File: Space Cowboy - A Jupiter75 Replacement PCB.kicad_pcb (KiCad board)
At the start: 2 copper layers, 303.5 x 119.5 mm, 237 parts, among them SW1 SW_PUSH, U1 ATmega32U4-AU, Y1 16MHz

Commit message: Update Space Cowboy - A Jupiter75 Replacement PCB.kicad_pcb
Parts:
- moved R4 46.2 mm to (160.3, 147.3), turned to 0 degrees
- moved C8 0.33 mm to (164.8, 144.3)
- moved C6 0.28 mm to (166.1, 153.8), turned to 0 degrees
- moved C7 0.28 mm to (166.1, 147.4)
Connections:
- DRGB1 pad 4DIN: RGB_DI_PIN -> (no net)
- DRGB18 pad 4DIN: (no net) -> RGB_DI_PIN
- U1 pad 10: ROW1 -> ROW0
- U1 pad 11: ROW2 -> ROW1
- U1 pad 9: ROW0 -> ROW2
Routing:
- net ROW0: track 285.8 -> 378.7 mm, vias 0 -> 2
- net ROW1: track 290.1 -> 360.3 mm, vias 0 -> 2
- net Net-(R4-Pad1): track 4.32 -> 62.0 mm, vias 0 -> 4
- net ROW2: track 276.8 -> 325.3 mm, vias 0 -> 2
- net ROW3: track 296.0 -> 330.0 mm, vias 0 -> 2
- net Net-(R2-Pad2): track 174.4 -> 200.6 mm, vias 2 -> 4
- net Net-(R3-Pad1): track 175.0 -> 200.9 mm, vias 2 -> 4
- net RGB_DI_PIN: track 0.00 -> 25.2 mm, vias 0 -> 2
- net ROW5: track 312.4 -> 336.1 mm, vias 2 -> 4
- net Net-(D46-Pad2): track 3.70 -> 20.5 mm, vias 0 -> 1
- net +5V: track 1139.8 -> 1154.1 mm, vias 12 -> 13
- net COL6: track 169.9 -> 157.1 mm
- net ROW4: track 296.5 -> 305.8 mm
- net GND: track 137.1 -> 142.1 mm
- net Net-(D31-Pad2): track 12.8 -> 14.0 mm, vias 0 -> 1
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- added copper zone on B.Cu, net GND

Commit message: Update Space Cowboy - A Jupiter75 Replacement PCB.kicad_pcb
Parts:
- moved R6 1.63 mm to (69.9, 52.6)
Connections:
- U1 pad TAB: (no net) -> GND
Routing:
- net GND: track 142.1 -> 516.7 mm, vias 2 -> 20
- net +5V: track 1154.1 -> 1165.3 mm
- net COL11: track 257.8 -> 255.8 mm
- net Net-(R6-Pad1): track 3.67 -> 5.29 mm
- net (no net): track 587.6 -> 586.8 mm
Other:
- board text added: "J.C.K. Revision 1.0 2021"

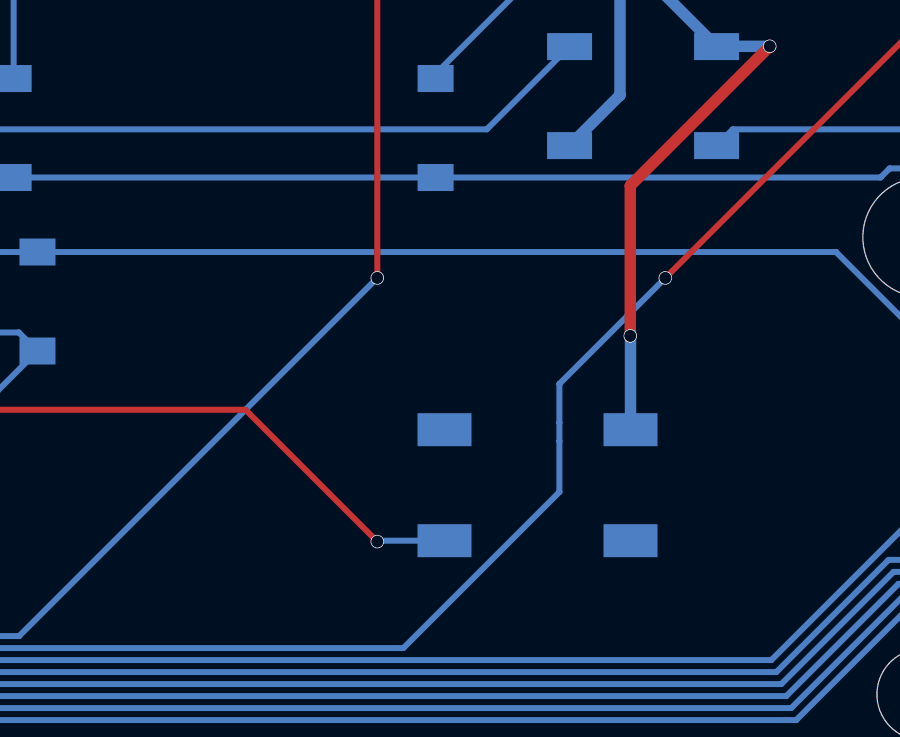
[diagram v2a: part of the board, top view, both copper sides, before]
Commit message: Update Space Cowboy - A Jupiter75 Replacement PCB.kicad_pcb
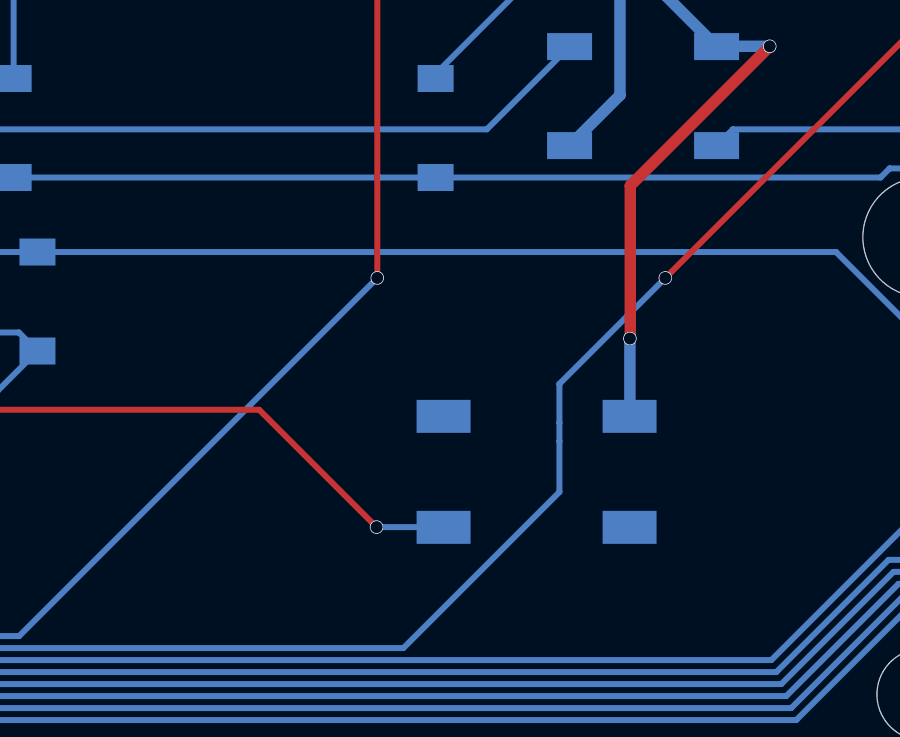
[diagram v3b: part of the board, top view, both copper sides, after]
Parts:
- added G***: LOGO, Graphics:Space Cowboy 2, B.Cu at (197.8, 159.4)
- moved SW1 0.45 mm to (213.5, 152.0)

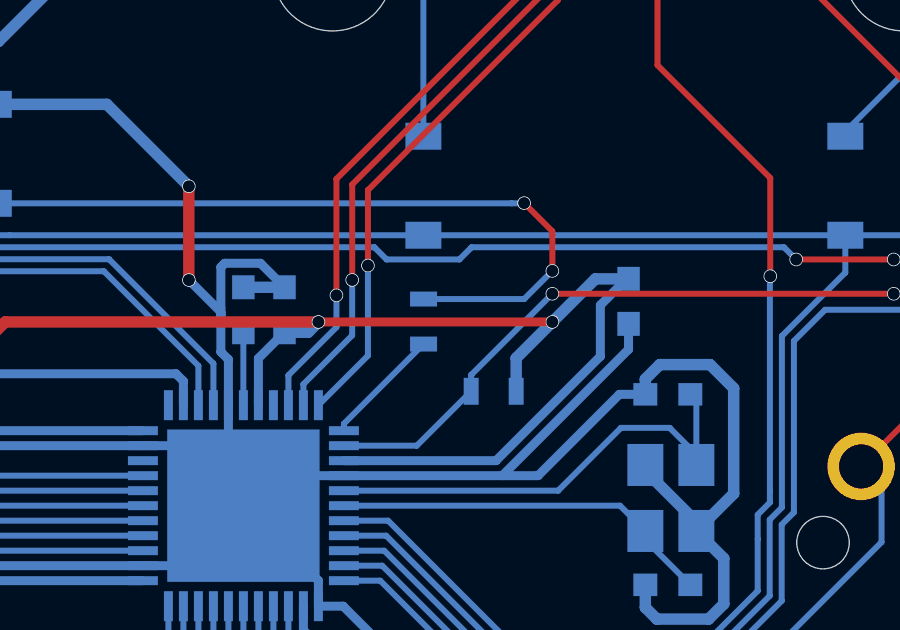
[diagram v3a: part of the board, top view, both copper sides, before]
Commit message: Update Space Cowboy - A Jupiter75 Replacement PCB.kicad_pcb
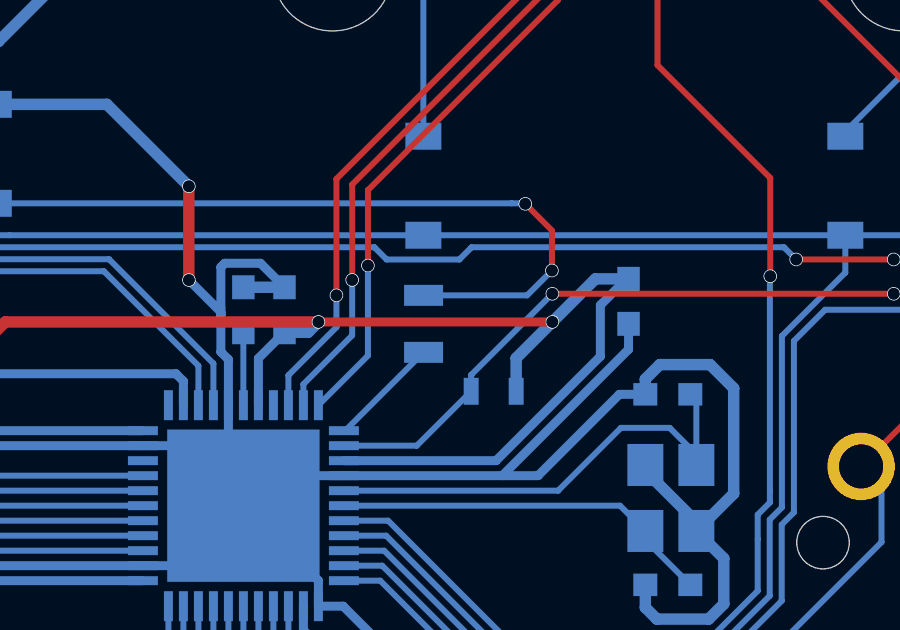
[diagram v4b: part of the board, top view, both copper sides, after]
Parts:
- R7: footprint Resistors_SMD:R_0603 -> Resistors_SMD:R_0805
- moved R7 0.08 mm to (158.0, 145.1)
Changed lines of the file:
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@@
     (thickness 1.6)
     (drawings 17)
-    (tracks 1684)
+    (tracks 1683)
     (zones 0)
     (modules 238)
@@
     (uvia_drill 0.1)
   )
+  (module Resistors_SMD:R_0805 (layer B.Cu)
+    (at 157.9626 145.0975 270)
+    (descr "Resistor SMD 0805, reflow soldering, Vishay (see dcrcw.pdf)")
+    (tags "resistor 0805")
+    (attr smd)
+    (fp_text reference R7 (at 0 1.45 90) (layer B.SilkS) hide
+      (effects (font (size 1 1) (thickness 0.15)) (justify mirror))
+    )
+    (fp_text value 0.5k (at 0 -1.5 90) (layer B.Fab) hide
+      (effects (font (size 1 1) (thickness 0.15)) (justify mirror))
+    )
+    (fp_line (start 1.55 -0.9) (end -1.55 -0.9) (layer B.CrtYd) (width 0.05))
+    (fp_line (start 1.55 -0.9) (end 1.55 0.9) (layer B.CrtYd) (width 0.05))
+    (fp_line (start -1.55 0.9) (end -1.55 -0.9) (layer B.CrtYd) (width 0.05))
+    (fp_line (start -1.55 0.9) (end 1.55 0.9) (layer B.CrtYd) (width 0.05))
+    (fp_line (start -0.6 0.88) (end 0.6 0.88) (layer B.SilkS) (width 0.12))
+    (fp_line (start 0.6 -0.88) (end -0.6 -0.88) (layer B.SilkS) (width 0.12))
+    (fp_line (start -1 0.62) (end 1 0.62) (layer B.Fab) (width 0.1))
+    (fp_line (start 1 0.62) (end 1 -0.62) (layer B.Fab) (width 0.1))
+    (fp_line (start 1 -0.62) (end -1 -0.62) (layer B.Fab) (width 0.1))
+    (fp_line (start -1 -0.62) (end -1 0.62) (layer B.Fab) (width 0.1))
+    (fp_text user %R (at 0.0007 0 90) (layer B.Fab)
+      (effects (font (size 0.4 0.4) (thickness 0.075)) (justify mirror))
+    )
+    (pad 1 smd rect (at -0.95 0 270) (size 0.7 1.3) (layers B.Cu B.Paste B.Mask)
+      (net 123 RGB_DI_PIN))
+    (pad 2 smd rect (at 0.95 0 270) (size 0.7 1.3) (layers B.Cu B.Paste B.Mask)
+      (net 124 "Net-(R7-Pad2)"))
+    (model ${KISYS3DMOD}/Resistors_SMD.3dshapes/R_0805.wrl
+      (at (xyz 0 0 0))
+      (scale (xyz 1 1 1))
+      (rotate (xyz 0 0 0))
+    )
+  )
   (module "Graphics:Space Cowboy 2" (layer B.Cu)
     (at 197.805 159.4485 180)
@@
   )
   (module Resistors_SMD:R_0603 (layer B.Cu)
-    (at 157.9626 145.0206 270)
-    (descr "Resistor SMD 0603, reflow soldering, Vishay (see dcrcw.pdf)")
-    (tags "resistor 0603")
-    (attr smd)
-    (fp_text reference R7 (at 0 1.45 90) (layer B.SilkS) hide
-      (effects (font (size 1 1) (thickness 0.15)) (justify mirror))
-    )
-    (fp_text value 0.5k (at 0 -1.5 90) (layer B.Fab)
-      (effects (font (size 1 1) (thickness 0.15)) (justify mirror))
-    )
-    (fp_line (start 1.25 -0.7) (end -1.25 -0.7) (layer B.CrtYd) (width 0.05))
-    (fp_line (start 1.25 -0.7) (end 1.25 0.7) (layer B.CrtYd) (width 0.05))
-    (fp_line (start -1.25 0.7) (end -1.25 -0.7) (layer B.CrtYd) (width 0.05))
-    (fp_line (start -1.25 0.7) (end 1.25 0.7) (layer B.CrtYd) (width 0.05))
-    (fp_line (start -0.5 0.68) (end 0.5 0.68) (layer B.SilkS) (width 0.12))
-    (fp_line (start 0.5 -0.68) (end -0.5 -0.68) (layer B.SilkS) (width 0.12))
-    (fp_line (start -0.8 0.4) (end 0.8 0.4) (layer B.Fab) (width 0.1))
-    (fp_line (start 0.8 0.4) (end 0.8 -0.4) (layer B.Fab) (width 0.1))
-    (fp_line (start 0.8 -0.4) (end -0.8 -0.4) (layer B.Fab) (width 0.1))
-    (fp_line (start -0.8 -0.4) (end -0.8 0.4) (layer B.Fab) (width 0.1))
-    (fp_text user %R (at 0.0007 0 90) (layer B.Fab)
-      (effects (font (size 0.4 0.4) (thickness 0.075)) (justify mirror))
-    )
-    (pad 1 smd rect (at -0.75 0 270) (size 0.5 0.9) (layers B.Cu B.Paste B.Mask)
-      (net 123 RGB_DI_PIN))
-    (pad 2 smd rect (at 0.75 0 270) (size 0.5 0.9) (layers B.Cu B.Paste B.Mask)
-      (net 124 "Net-(R7-Pad2)"))
-    (model ${KISYS3DMOD}/Resistors_SMD.3dshapes/R_0603.wrl
-      (at (xyz 0 0 0))
-      (scale (xyz 1 1 1))
-      (rotate (xyz 0 0 0))
-    )
-  )
-  (module Resistors_SMD:R_0603 (layer B.Cu)
     (at 69.862 52.6288)
     (descr "Resistor SMD 0603, reflow soldering, Vishay (see dcrcw.pdf)")
@@
   (segment (start 68.298 50.1892) (end 69.112 51.0032) (width 0.2) (layer B.Cu) (net 122))
   (segment (start 68.298 47.6746) (end 68.298 50.1892) (width 0.2) (layer B.Cu) (net 122))
-  (via (at 162.2552 143.3322) (size 0.45) (drill 0.4) (layers F.Cu B.Cu) (net 123))
-  (segment (start 161.3168 144.2706) (end 162.2552 143.3322) (width 0.2) (layer B.Cu) (net 123))
-  (segment (start 157.9626 144.2706) (end 161.3168 144.2706) (width 0.2) (layer B.Cu) (net 123))
-  (segment (start 162.2552 143.3322) (end 162.2552 142.1384) (width 0.2) (layer F.Cu) (net 123))
   (segment (start 143.4875 141.08) (end 160.9006 141.08) (width 0.2) (layer B.Cu) (net 123))
-  (via (at 161.3154 141.0716) (size 0.45) (drill 0.4) (layers F.Cu B.Cu) (net 123))
-  (segment (start 161.307 141.08) (end 161.3154 141.0716) (width 0.2) (layer B.Cu) (net 123))
-  (segment (start 160.9006 141.08) (end 161.307 141.08) (width 0.2) (layer B.Cu) (net 123))
-  (segment (start 162.2552 142.0114) (end 162.2552 142.1384) (width 0.2) (layer F.Cu) (net 123))
-  (segment (start 161.3154 141.0716) (end 162.2552 142.0114) (width 0.2) (layer F.Cu) (net 123))
-  (segment (start 155.3074 148.4258) (end 157.9626 145.7706) (width 0.2) (layer B.Cu) (net 124))
-  (segment (start 155.3074 148.6582) (end 155.3074 148.4258) (width 0.2) (layer B.Cu) (net 124))
+  (via (at 162.2425 143.3195) (size 0.45) (drill 0.4) (layers F.Cu B.Cu) (net 123))
+  (segment (start 161.4145 144.1475) (end 162.2425 143.3195) (width 0.2) (layer B.Cu) (net 123))
+  (segment (start 157.9626 144.1475) (end 161.4145 144.1475) (width 0.2) (layer B.Cu) (net 123))
+  (via (at 161.3535 141.097) (size 0.45) (drill 0.4) (layers F.Cu B.Cu) (net 123))
+  (segment (start 161.3365 141.08) (end 161.3535 141.097) (width 0.2) (layer B.Cu) (net 123))
+  (segment (start 160.9006 141.08) (end 161.3365 141.08) (width 0.2) (layer B.Cu) (net 123))
+  (segment (start 162.2425 141.986) (end 161.3535 141.097) (width 0.2) (layer F.Cu) (net 123))
+  (segment (start 162.2425 143.3195) (end 162.2425 141.986) (width 0.2) (layer F.Cu) (net 123))
+  (segment (start 155.3519 148.6582) (end 157.9626 146.0475) (width 0.2) (layer B.Cu) (net 124))
+  (segment (start 155.3074 148.6582) (end 155.3519 148.6582) (width 0.2) (layer B.Cu) (net 124))
   (zone (net 2) (net_name GND) (layer B.Cu) (hatch edge 0.508)
     (connect_pads (clearance 0.02))
